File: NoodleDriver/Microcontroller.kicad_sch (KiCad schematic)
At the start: 7 parts, among them J5 USB_C_Receptacle_USB2.0_16P, U6 CH32V203F8U6

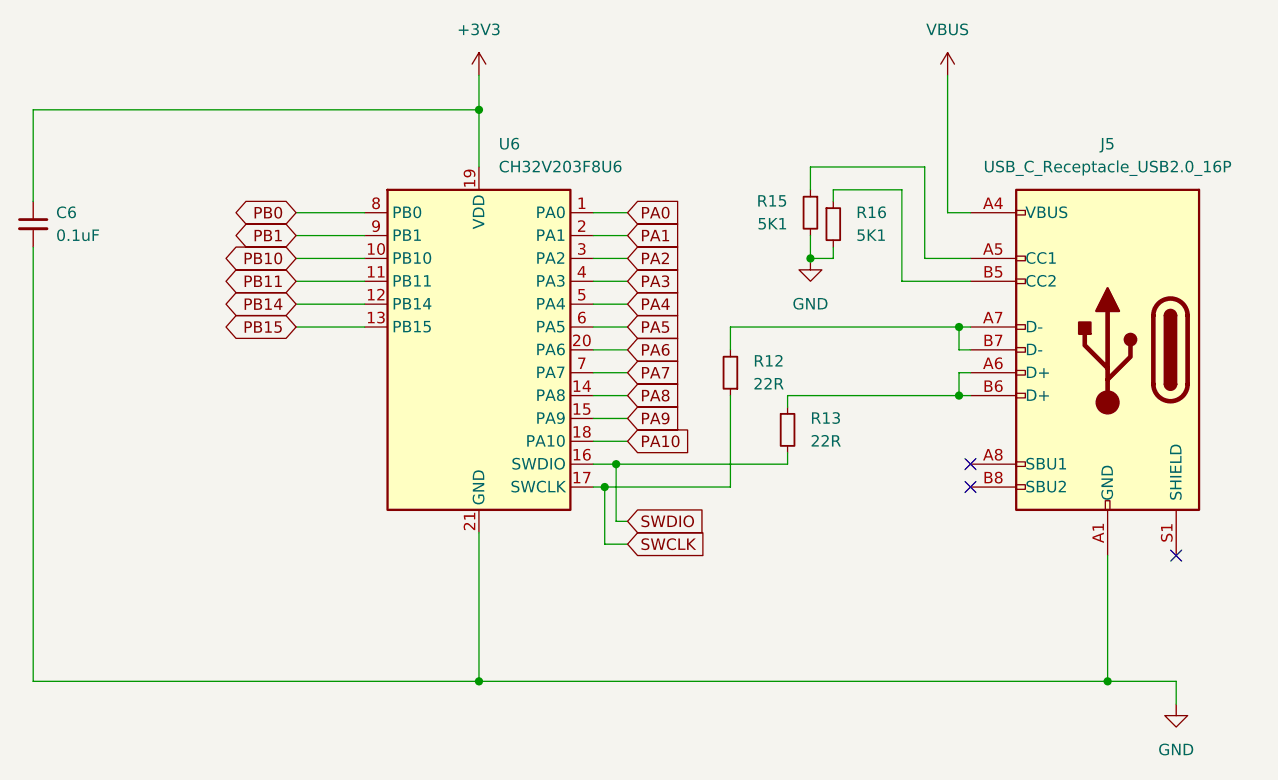
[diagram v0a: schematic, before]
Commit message: Final tuning of prototype board, which we've ordered a handful of prototypes to be fabbed.  Part of #8
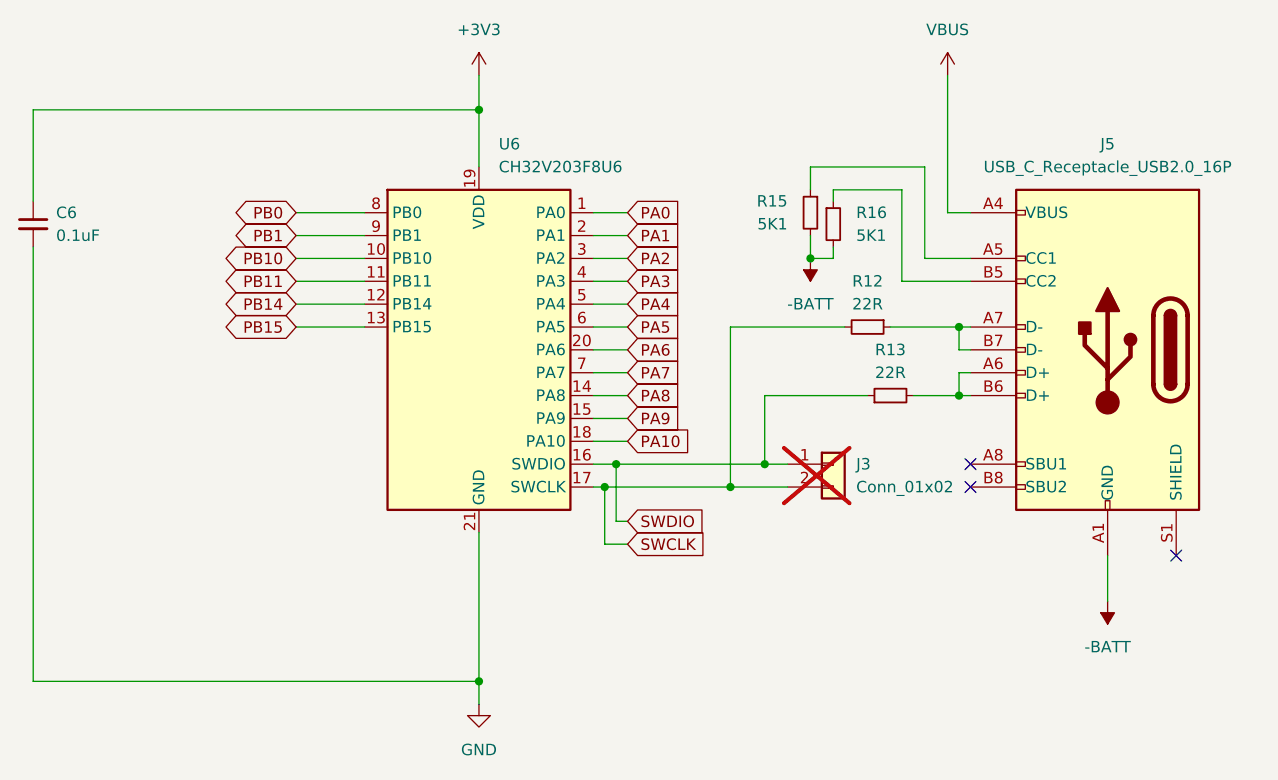
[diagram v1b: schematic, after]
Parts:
- added J3: Conn_01x02, Connector_PinSocket_2.54mm:PinSocket_1x02_P2.54mm_Vertical, symbol Connector_Generic:Conn_01x02
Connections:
- net GND: no longer J5.A1 (GND), J5.A12 (GND), J5.B1 (GND), J5.B12 (GND), R15.2, R16.2
- net SWCLK: now also R12.2, J3.2 (Pin_2); no longer R12.1
- net SWDIO: now also R13.1, J3.1 (Pin_1); no longer R13.2
- net at J5.A6 (D+), J5.B6 (D+): now also R13.2; no longer R13.1
- net at J5.A7 (D-), J5.B7 (D-): now also R12.1; no longer R12.2
- new net -BATT: J5.A1 (GND), J5.A12 (GND), J5.B1 (GND), J5.B12 (GND), R15.2, R16.2
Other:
- moved on the sheet: R12, R13
